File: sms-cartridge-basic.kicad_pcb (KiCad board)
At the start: 2 copper layers, 65.8 x 38.5 mm, 5 parts, among them U1 27C256, U2 SMSUCartEdge

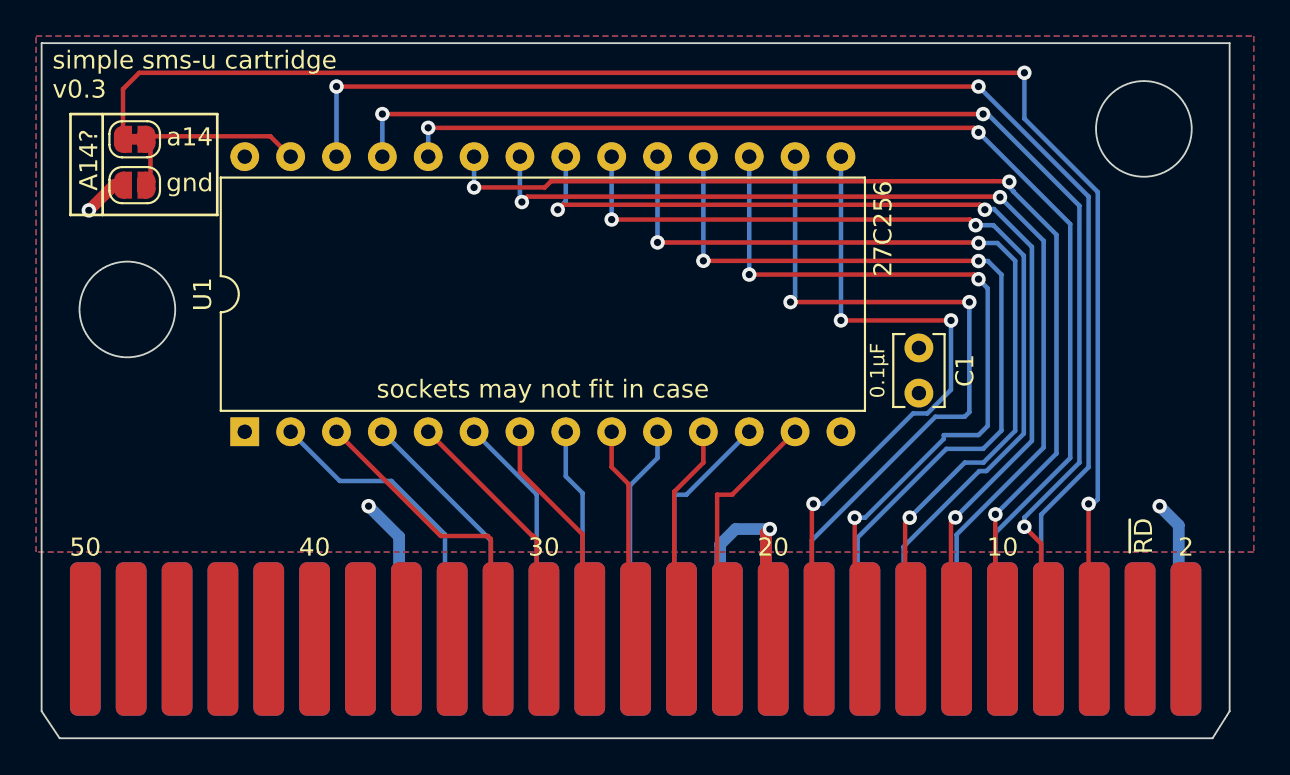
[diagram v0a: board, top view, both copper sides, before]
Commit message: 27c64 support
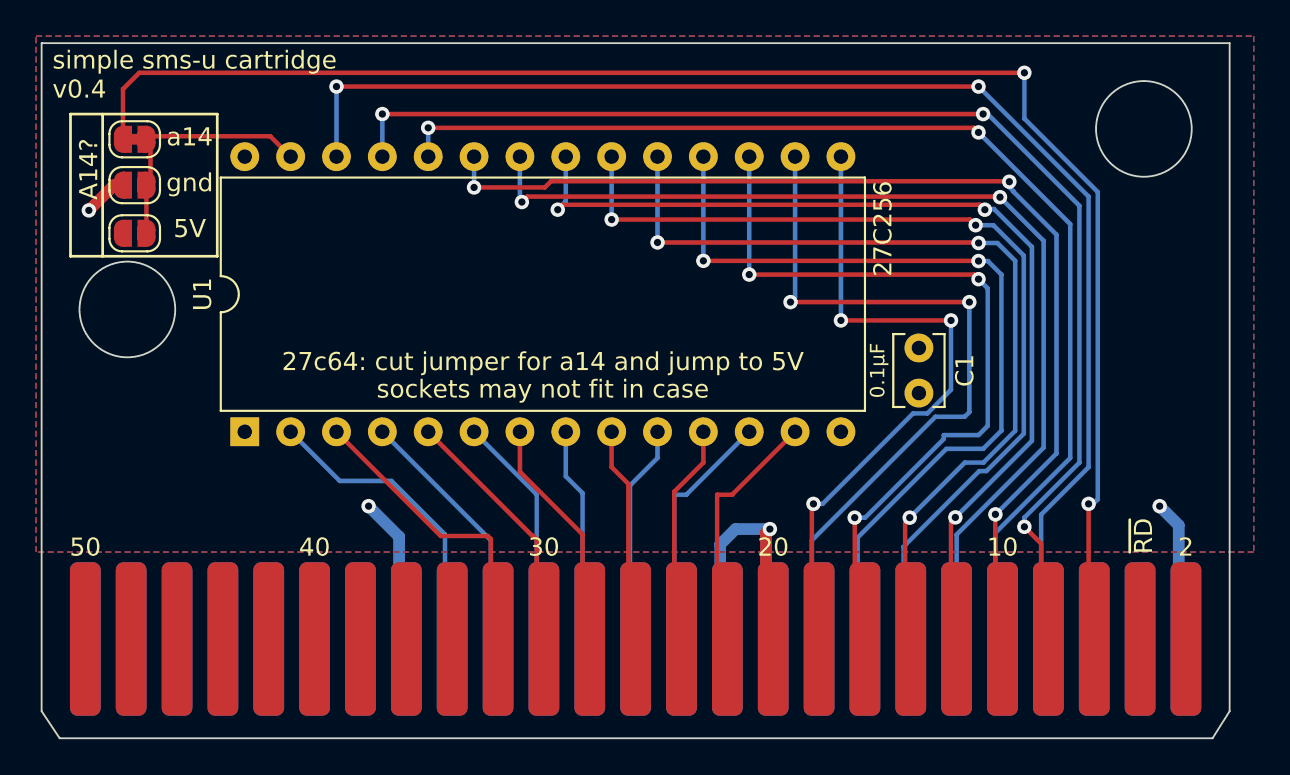
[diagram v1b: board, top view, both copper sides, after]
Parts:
- added JP3: Jumper_2_Open, Jumper:SolderJumper-2_P1.3mm_Open_RoundedPad1.0x1.5mm, F.Cu at (105.2, 65.5)
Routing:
- net Net-(JP1-Pad2): track 10.8 -> 13.5 mm
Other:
- board text added: "27c64: cut jumper for a14 and jump to 5V"
- board text added: "5V"
- board text added: "simple sms-u cartridge v0.4"
- board text removed: "simple sms-u cartridge v0.3"
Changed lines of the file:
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@@
       (net 48 "unconnected-(U2-Pad50)") (pinfunction "~{NMI}") (pintype "input+no_connect"))
+  )
+  (footprint "Jumper:SolderJumper-2_P1.3mm_Open_RoundedPad1.0x1.5mm" (layer "F.Cu")
+    (at 105.156 65.532)
+    (descr "SMD Solder Jumper, 1x1.5mm, rounded Pads, 0.3mm gap, open")
+    (tags "solder jumper open")
+    (property "Sheetfile" "sms-cartridge-basic.kicad_sch")
+    (property "Sheetname" "")
+    (attr exclude_from_pos_files)
+    (fp_text reference "JP3" (at 0 -1.8) (layer "F.SilkS") hide
+      (effects (font (size 1 1) (thickness 0.15)))
+    )
+    (fp_text value "Jumper_2_Open" (at 0 1.9) (layer "F.Fab")
+      (effects (font (size 1 1) (thickness 0.15)))
+    )
+    (fp_line (start 0.7 1) (end -0.7 1) (layer "F.SilkS") (width 0.12))
+    (fp_line (start -1.4 0.3) (end -1.4 -0.3) (layer "F.SilkS") (width 0.12))
+    (fp_line (start 1.4 -0.3) (end 1.4 0.3) (layer "F.SilkS") (width 0.12))
+    (fp_line (start -0.7 -1) (end 0.7 -1) (layer "F.SilkS") (width 0.12))
+    (fp_arc (start 1.4 0.3) (mid 1.194975 0.794975) (end 0.7 1) (layer "F.SilkS") (width 0.12))
+    (fp_arc (start 0.7 -1) (mid 1.194975 -0.794975) (end 1.4 -0.3) (layer "F.SilkS") (width 0.12))
+    (fp_arc (start -1.4 -0.3) (mid -1.194975 -0.794975) (end -0.7 -1) (layer "F.SilkS") (width 0.12))
+    (fp_arc (start -0.7 1) (mid -1.194975 0.794975) (end -1.4 0.3) (layer "F.SilkS") (width 0.12))
+    (fp_line (start -1.65 -1.25) (end 1.65 -1.25) (layer "F.CrtYd") (width 0.05))
+    (fp_line (start 1.65 1.25) (end -1.65 1.25) (layer "F.CrtYd") (width 0.05))
+    (fp_line (start 1.65 1.25) (end 1.65 -1.25) (layer "F.CrtYd") (width 0.05))
+    (fp_line (start -1.65 -1.25) (end -1.65 1.25) (layer "F.CrtYd") (width 0.05))
+    (pad "1" smd custom (at -0.65 0) (size 1 0.5) (layers "F.Cu" "F.Mask")
+      (net 1 "+5V") (pinfunction "A") (pintype "passive") (zone_connect 2)
+      (options (clearance outline) (anchor rect))
+      (primitives
+        (gr_circle (center 0 0.25) (end 0.5 0.25) (width 0) (fill yes))
+        (gr_circle (center 0 -0.25) (end 0.5 -0.25) (width 0) (fill yes))
+        (gr_poly (pts
+            (xy 0.5 0.75)
+            (xy 0 0.75)
+            (xy 0 -0.75)
+            (xy 0.5 -0.75)
+          ) (width 0) (fill yes))
+      ))
+    (pad "2" smd custom (at 0.65 0) (size 1 0.5) (layers "F.Cu" "F.Mask")
+      (net 4 "Net-(JP1-Pad2)") (pinfunction "B") (pintype "passive") (zone_connect 2)
+      (options (clearance outline) (anchor rect))
+      (primitives
+        (gr_circle (center 0 0.25) (end 0.5 0.25) (width 0) (fill yes))
+        (gr_circle (center 0 -0.25) (end 0.5 -0.25) (width 0) (fill yes))
+        (gr_poly (pts
+            (xy 0 0.75)
+            (xy -0.5 0.75)
+            (xy -0.5 -0.75)
+            (xy 0 -0.75)
+          ) (width 0) (fill yes))
+      ))
   )
   (footprint "Capacitor_THT:C_Disc_D3.8mm_W2.6mm_P2.50mm" (layer "F.Cu")
@@
     )
   )
-  (gr_line (start 103.378 58.928) (end 103.378 64.516) (layer "F.SilkS") (width 0.15))
-  (gr_rect (start 101.6 58.928) (end 109.728 64.516) (layer "F.SilkS") (width 0.15) (fill none))
+  (gr_line (start 103.378 58.928) (end 103.378 66.802) (layer "F.SilkS") (width 0.15))
+  (gr_rect (start 101.6 58.928) (end 109.728 66.802) (layer "F.SilkS") (width 0.15) (fill none))
   (gr_rect (start 166 93.9) (end 99.2 83.754) (layer "B.Mask") (width 0.15) (fill solid))
   (gr_rect (start 166 93.9) (end 99.2 83.754) (layer "F.Mask") (width 0.15) (fill solid))
@@
     (effects (font (size 1 1) (thickness 0.15)) (justify mirror))
   )
+  (gr_text "5V" (at 108.204 65.278) (layer "F.SilkS")
+    (effects (font (size 1 1) (thickness 0.15)))
+  )
+  (gr_text "27c64: cut jumper for a14 and jump to 5V" (at 127.762 72.644) (layer "F.SilkS")
+    (effects (font (size 1 1) (thickness 0.15)))
+  )
   (gr_text "~{RD}" (at 161.036 82.296 90) (layer "F.SilkS")
     (effects (font (size 1 1) (thickness 0.15)))
   )
-  (gr_text "A14?" (at 102.616 61.468 90) (layer "F.SilkS")
-    (effects (font (size 1 1) (thickness 0.15)))
-  )
-  (gr_text "simple sms-u cartridge\nv0.3" (at 100.6 56.75) (layer "F.SilkS")
+  (gr_text "A14?" (at 102.616 61.976 90) (layer "F.SilkS")
+    (effects (font (size 1 1) (thickness 0.15)))
+  )
+  (gr_text "simple sms-u cartridge\nv0.4" (at 100.6 56.75) (layer "F.SilkS")
     (effects (font (size 1 1) (thickness 0.15)) (justify left))
   )
@@
   (segment (start 158.496 63.246) (end 158.496 80.264) (width 0.25) (layer "B.Cu") (net 3))
   (segment (start 106.194511 60.160489) (end 112.667489 60.160489) (width 0.25) (layer "F.Cu") (net 4))
+  (segment (start 105.806 65.532) (end 105.806 62.865) (width 0.25) (layer "F.Cu") (net 4))
   (segment (start 106.03 60.325) (end 106.03 62.85) (width 0.25) (layer "F.Cu") (net 4))
   (segment (start 106.03 60.325) (end 106.194511 60.160489) (width 0.25) (layer "F.Cu") (net 4))
